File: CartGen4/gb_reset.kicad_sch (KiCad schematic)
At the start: 2 parts

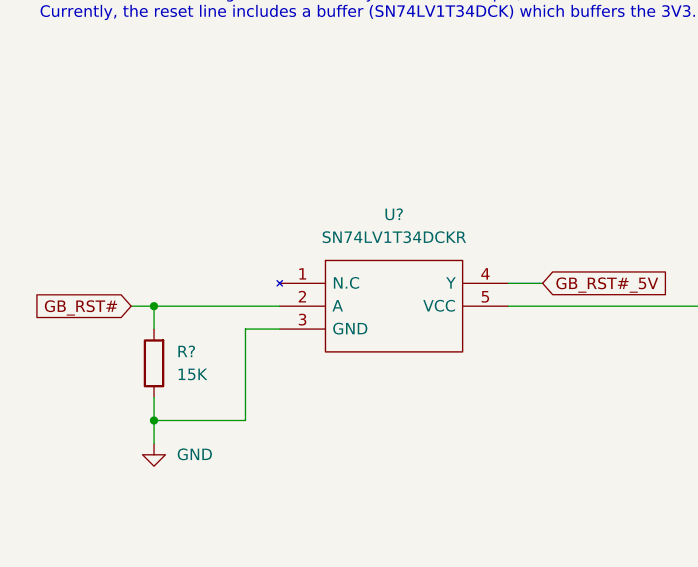
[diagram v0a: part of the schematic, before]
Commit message: Added FPGA and RAM symbols
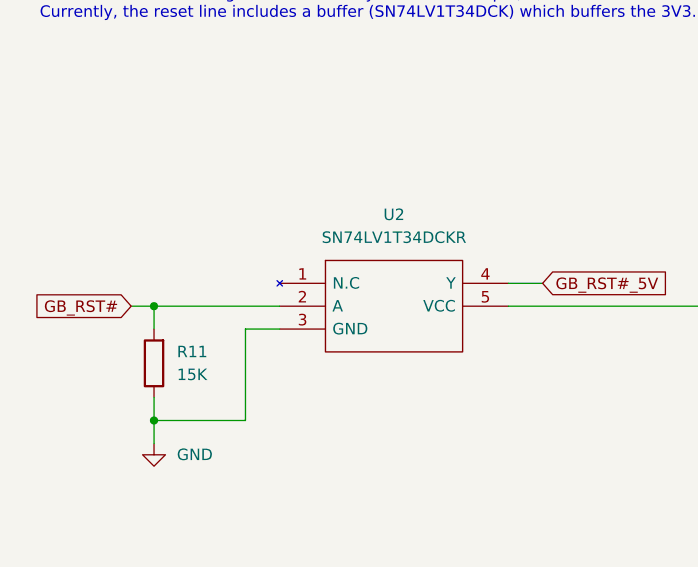
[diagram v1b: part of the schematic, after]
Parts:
- gave numbers to parts that had none: 2
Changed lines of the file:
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@@
     )
   )
-  (symbol (lib_id "power:+3V3") (at 127 107.95 0)
+  (symbol (lib_id "power:+3V3") (at 127 107.95 0) (unit 1)
     (in_bom yes) (on_board yes) (fields_autoplaced)
-    (property "Reference" "#PWR?" (id 0) (at 127 111.76 0)
+    (property "Reference" "#PWR031" (id 0) (at 127 111.76 0)
       (effects (font (size 1.27 1.27)) hide)
     )
@@
     (pin "1")
   )
-  (symbol (lib_id "SamacSys_Parts:SN74LV1T34DCKR") (at 73.66 107.95 0)
+  (symbol (lib_id "SamacSys_Parts:SN74LV1T34DCKR") (at 73.66 107.95 0) (unit 1)
     (in_bom yes) (on_board yes)
-    (property "Reference" "U?" (id 0) (at 86.36 100.33 0))
+    (property "Reference" "U2" (id 0) (at 86.36 100.33 0))
     (property "Value" "SN74LV1T34DCKR" (id 1) (at 86.36 102.87 0))
     (property "Footprint" "SOT65P210X110-5N" (id 2) (at 95.25 105.41 0)
@@
     (pin "5")
   )
-  (symbol (lib_id "power:GND") (at 59.69 125.73 0)
+  (symbol (lib_id "power:GND") (at 59.69 125.73 0) (unit 1)
     (in_bom yes) (on_board yes) (fields_autoplaced)
-    (property "Reference" "#PWR?" (id 0) (at 59.69 132.08 0)
+    (property "Reference" "#PWR030" (id 0) (at 59.69 132.08 0)
       (effects (font (size 1.27 1.27)) hide)
     )
@@
     (pin "1")
   )
-  (symbol (lib_id "Device:R") (at 59.69 116.84 180)
+  (symbol (lib_id "Device:R") (at 59.69 116.84 180) (unit 1)
     (in_bom yes) (on_board yes) (fields_autoplaced)
-    (property "Reference" "R?" (id 0) (at 62.23 115.5699 0)
+    (property "Reference" "R11" (id 0) (at 62.23 115.5699 0)
       (effects (font (size 1.27 1.27)) (justify right))
     )
